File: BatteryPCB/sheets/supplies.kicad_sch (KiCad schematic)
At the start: 6 parts, among them J5 to COTS altimeter, J6 to SRAD flight computer, SW2 COTS ARM, SW3 SRAD ARM

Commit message: Battery PCB schematic: ESP32, camera and pack-sense sheets merged; C9/C10 on the buck output
Schematic only: sheets 3-5 become one wired sheet (3. ESP32 + camera), C9/C10 move
to the buck sheet's +5V output, supplies renumbered 6 -> 4. Every connection,
part, value and footprint is unchanged; the board only gets the new sheet paths
and net-name prefixes (tools/sync_from_sch.py). Gerbers and drills are
geometrically identical to v22. DRC 0 with schematic parity.

Co-Authored-By: Claude Opus 5.5 <noreply@anthropic.com>
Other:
- title: 6. Independent 1S supplies -> 4. Independent 1S supplies
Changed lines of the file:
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@@
 	(paper "A4")
 	(title_block
-		(title "6. Independent 1S supplies")
+		(title "4. Independent 1S supplies")
 		(rev "A")
 		(company "Stanford SSI")
@@
 	(wire
 		(pts
-			(xy 44.45 54.61) (xy 44.45 49.53)
+			(xy 44.45 54.61)
+			(xy 44.45 49.53)
 		)
 		(stroke
@@
 	(wire
 		(pts
-			(xy 44.45 118.11) (xy 44.45 123.19)
+			(xy 44.45 118.11)
+			(xy 44.45 123.19)
 		)
 		(stroke
@@
 	(wire
 		(pts
-			(xy 149.86 110.49) (xy 144.78 110.49)
+			(xy 149.86 110.49)
+			(xy 144.78 110.49)
 		)
 		(stroke
@@
 	(wire
 		(pts
-			(xy 100.33 54.61) (xy 105.41 54.61)
+			(xy 100.33 54.61)
+			(xy 105.41 54.61)
 		)
 		(stroke
@@
 	(wire
 		(pts
-			(xy 44.45 110.49) (xy 44.45 105.41)
+			(xy 44.45 110.49)
+			(xy 44.45 105.41)
 		)
 		(stroke
@@
 	(wire
 		(pts
-			(xy 149.86 113.03) (xy 144.78 113.03)
+			(xy 149.86 113.03)
+			(xy 144.78 113.03)
 		)
 		(stroke
@@
 	(wire
 		(pts
-			(xy 149.86 54.61) (xy 144.78 54.61)
+			(xy 149.86 54.61)
+			(xy 144.78 54.61)
 		)
 		(stroke
@@
 	(wire
 		(pts
-			(xy 90.17 54.61) (xy 85.09 54.61)
+			(xy 90.17 54.61)
+			(xy 85.09 54.61)
 		)
 		(stroke
@@
 	(wire
 		(pts
-			(xy 149.86 57.15) (xy 144.78 57.15)
+			(xy 149.86 57.15)
+			(xy 144.78 57.15)
 		)
 		(stroke
@@
 	(wire
 		(pts
-			(xy 100.33 110.49) (xy 105.41 110.49)
+			(xy 100.33 110.49)
+			(xy 105.41 110.49)
 		)
 		(stroke
@@
 	(wire
 		(pts
-			(xy 90.17 110.49) (xy 85.09 110.49)
+			(xy 90.17 110.49)
+			(xy 85.09 110.49)
 		)
 		(stroke
@@
 	(wire
 		(pts
-			(xy 44.45 62.23) (xy 44.45 67.31)
+			(xy 44.45 62.23)
+			(xy 44.45 67.31)
 		)
 		(stroke

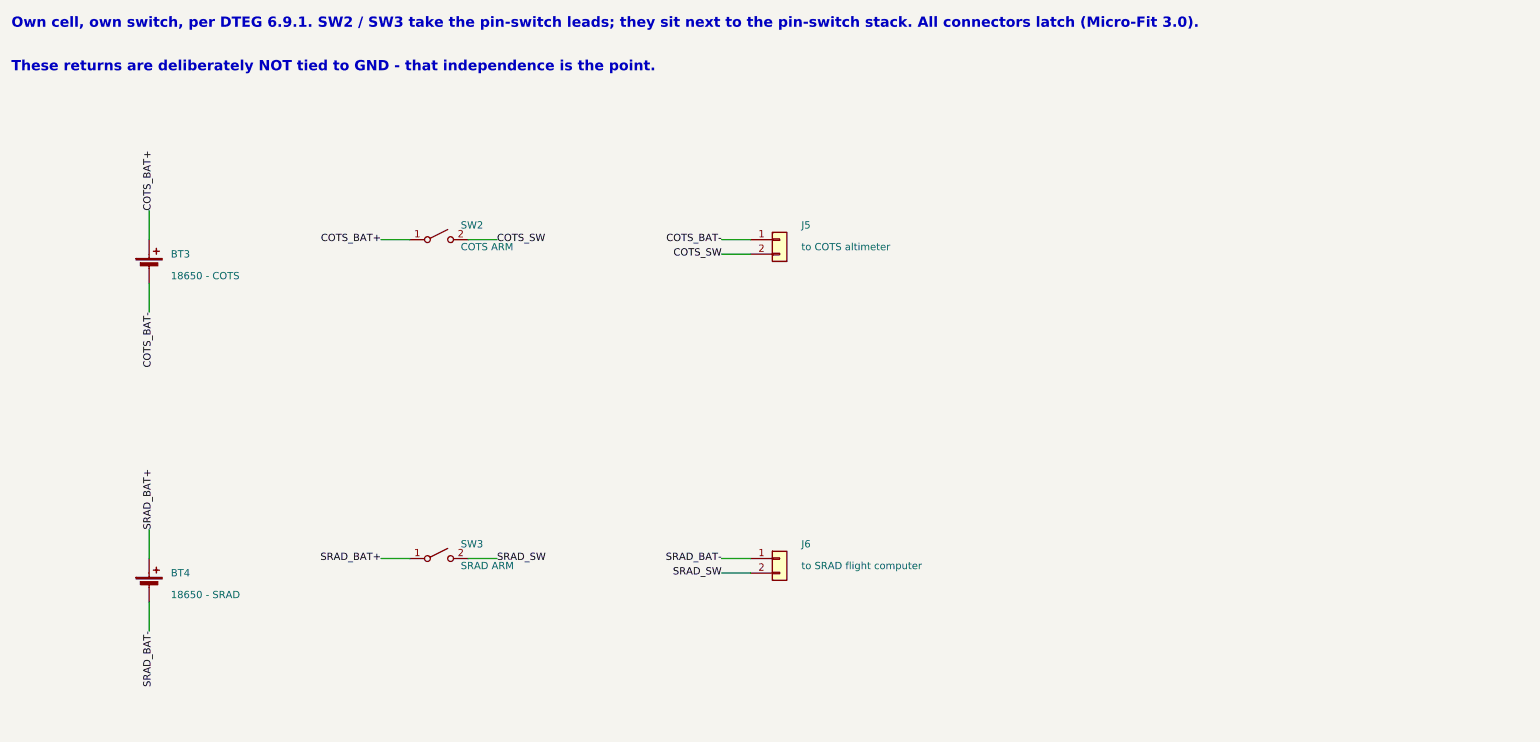
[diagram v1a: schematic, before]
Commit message: Battery PCB: schematic sheets re-saved after cleanup; board net names re-escaped
Same design as 428171c: identical netlist (42 parts, 55 nets, same pins,
values, footprints and MPNs) and identical board geometry. The board only
changes the sheet-name escaping inside net names ("COTS / SRAD" ->
"COTS {slash} SRAD").

Checks on this commit: ERC 0 errors; strict DRC 0 violations, 0 unconnected,
0 schematic parity issues (also with zones refilled); verify_A.py ALL PASS.
New ERC warnings: 16 endpoint_off_grid on the root and COTS/SRAD sheets
(half-grid wire ends and J6 pin 1); connectivity is unaffected.

Co-Authored-By: Claude Opus 5.5 <noreply@anthropic.com>
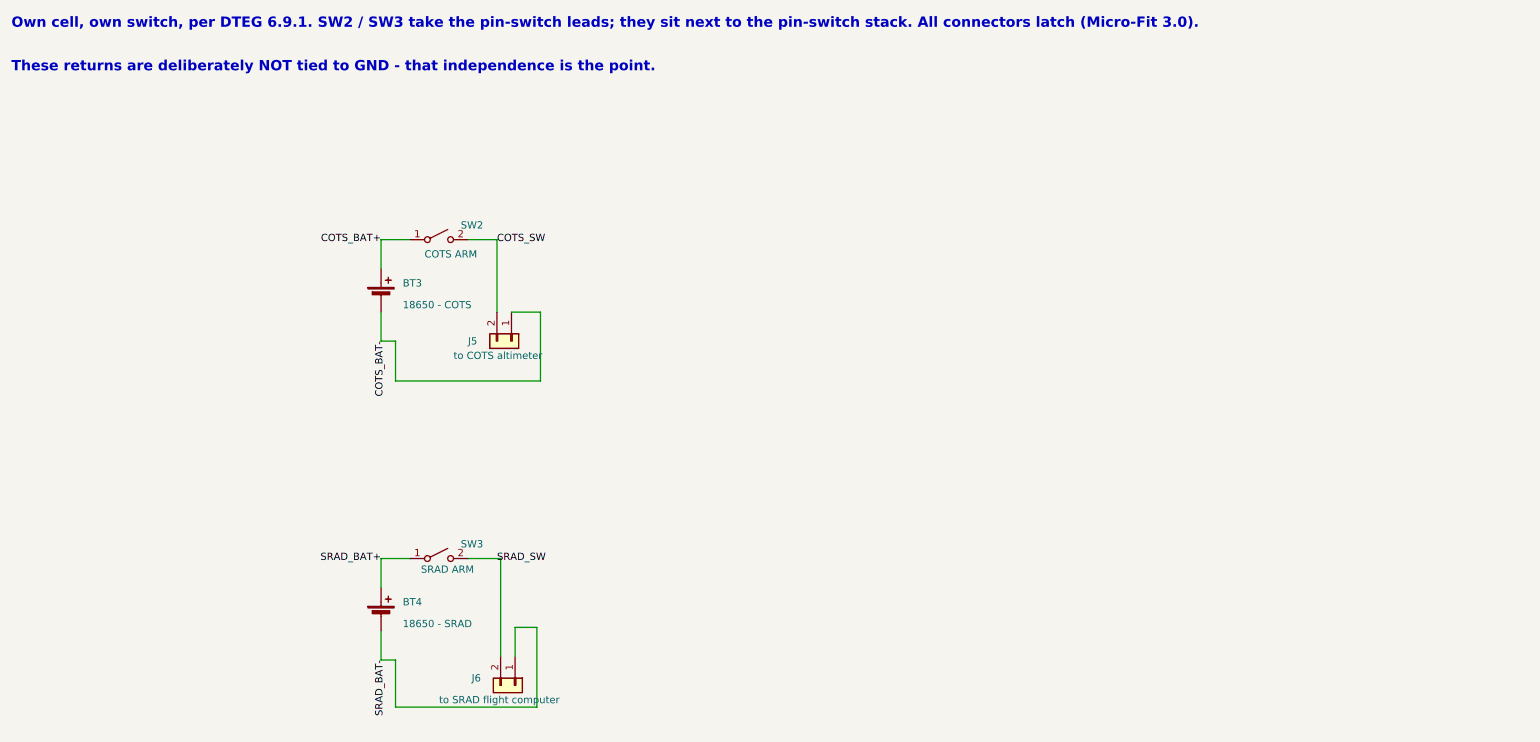
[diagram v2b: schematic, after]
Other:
- moved on the sheet: BT3, BT4, J5, J6
